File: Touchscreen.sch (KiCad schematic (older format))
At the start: 4 parts, among them P4 4pin_Cvilux_1_0mm

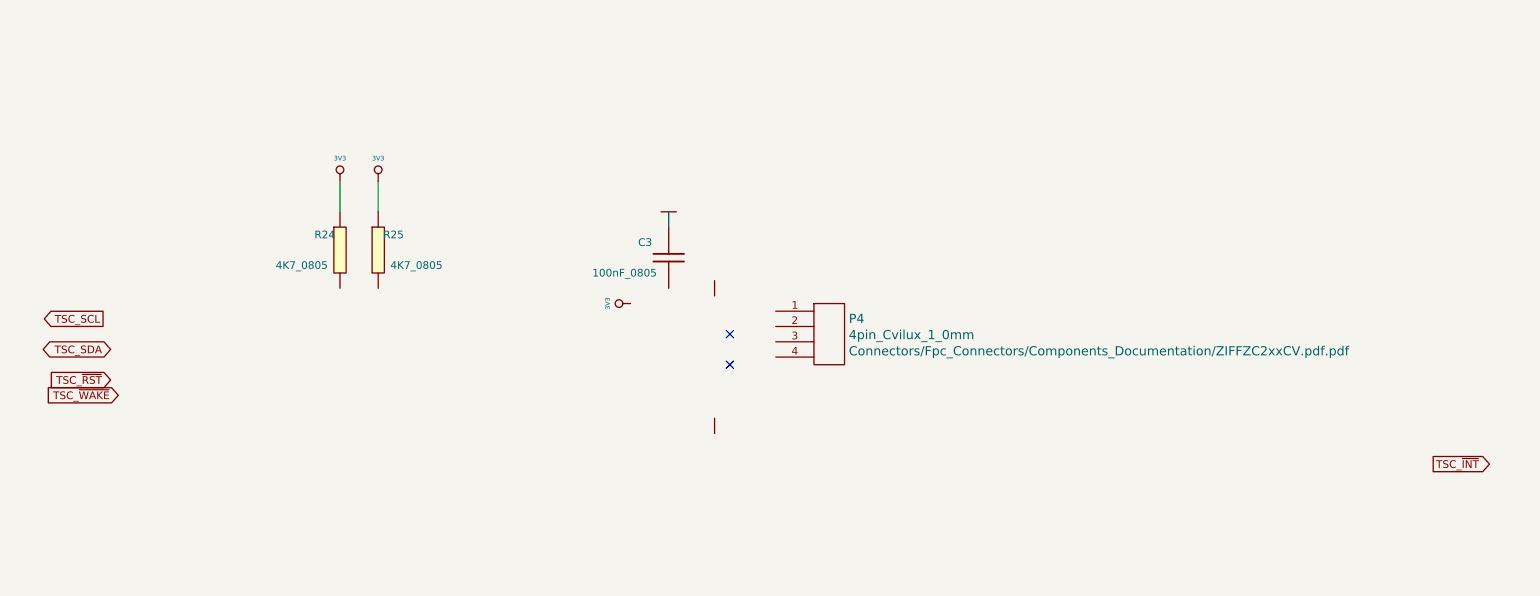
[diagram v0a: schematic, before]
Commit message: Schematic finished, needes to be rechecked, pcb finished needes to be tweeked
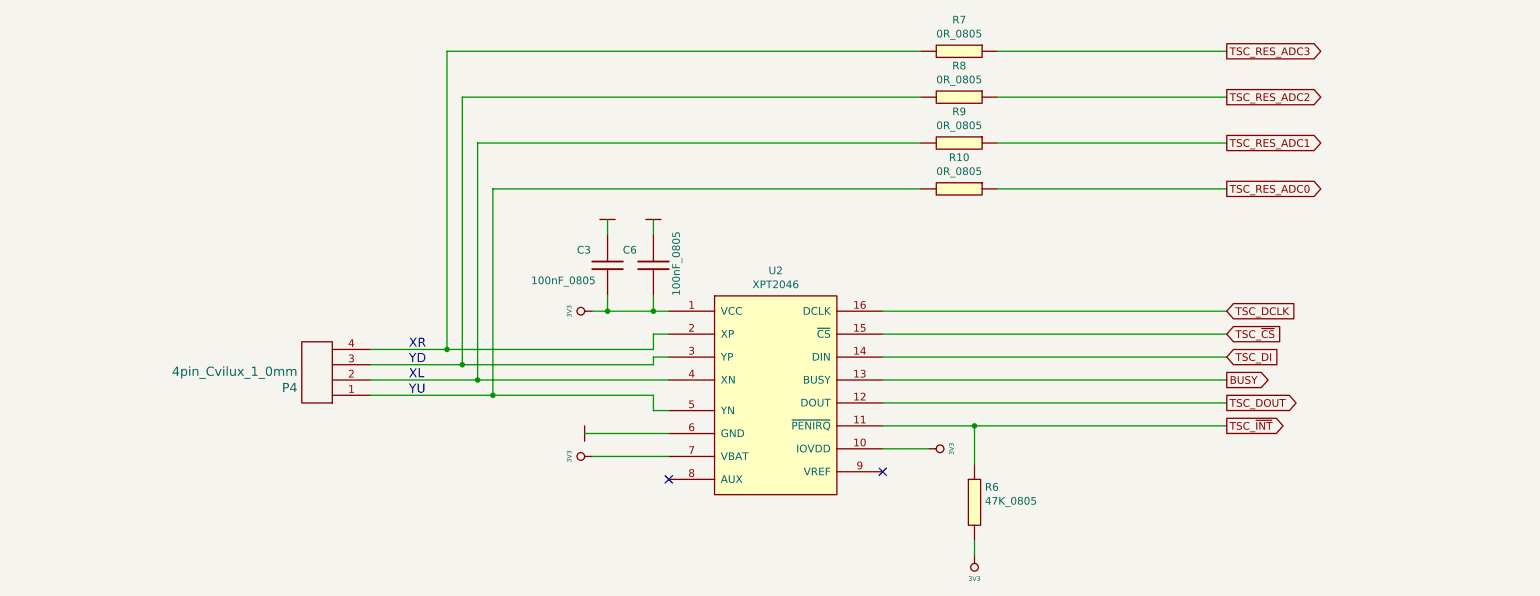
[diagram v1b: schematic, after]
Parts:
- removed R24, R25: 4K7_0805, Resistor_Smd_0805:4k7_0805, symbol 4K7_0805
- added C6: 100nF_0805, Capacitors_Smd_0805:100nF_0805, symbol 100nF_0805
- added R10, R7, R8, R9: 0R_0805, Resistor_Smd_0805:0R_0805, symbol 0R_0805
- added R6: 47K_0805, Resistor_Smd_0805:47k_0805, symbol 47K_0805
- added U2: XPT2046, Touch_Sensors:XPT2046_TSSOP16, symbol XPT2046
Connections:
- net 3V3: now also C3.2, C6.2, R6.2, U2.1 (VCC), U2.10 (IOVDD), U2.7 (VBAT)
- net GND: now also C6.1, U2.6 (GND)
- net TSC_~INT: now also R6.1, U2.11 (~PENIRQ)
- net at P4.1 (P1): now also R10.2, U2.5 (YN)
- net at P4.2 (P2): now also R9.2, U2.4 (XN)
- net at P4.3 (P3): now also R8.2, U2.3 (YP)
- net at P4.4 (P4): now also R7.2, U2.2 (XP)
- new net BUSY: U2.13 (BUSY)
- new net TSC_DCLK: U2.16 (DCLK)
- new net TSC_DI: U2.14 (DIN)
- new net TSC_DOUT: U2.12 (DOUT)
- new net TSC_RES_ADC0: R10.1
- new net TSC_RES_ADC1: R9.1
- new net TSC_RES_ADC2: R8.1
- new net TSC_RES_ADC3: R7.1
- new net TSC_~CS: U2.15 (~CS)
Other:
- note added: "XL"
- note added: "XR"
- note added: "YD"
- note added: "YU"
- moved on the sheet: C3, P4

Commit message: Corrected FPC 40pin top 0.5mm connector, generated again gerber and ps files
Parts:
- C3, C6: symbol 100nF_0805 -> Capacitors_Smd0805:100nF_0805
- P4: symbol 4pin_Cvilux_1_0mm -> Fpc_Connectors:4pin_Cvilux_1_0mm
- R10, R7, R8, R9: symbol 0R_0805 -> Resistors_Smd0805:0R_0805
- R6: symbol 47K_0805 -> Resistors_Smd0805:47K_0805
- U2: symbol XPT2046 -> Touch_Sensors:XPT2046
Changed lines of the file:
@@
-EESchema Schematic File Version 3
-LIBS:Capacitors_Smd0805
-LIBS:Capacitors_Smd_Tantal
-LIBS:Fpc_Connectors
-LIBS:Switching_Regulators
-LIBS:Diodes
-LIBS:Inductors
-LIBS:power
-LIBS:Resistors_Smd0603
-LIBS:Resistors_Smd0805
-LIBS:Symbols
-LIBS:Touch_Sensors
+EESchema Schematic File Version 4
 LIBS:TFT_LCD_4_3_AM480272H2T_V1_0-cache
 EELAYER 26 0
@@
 NoConn ~ 5200 4500
 $Comp
-L GND #PWR017
+L power1:GND #PWR017
 U 1 1 57E98920
 P 4650 4200
@@
 $EndComp
 $Comp
-L 3V3 #PWR018
+L power1:3V3 #PWR018
 U 1 1 57E99C42
 P 4700 4350
@@
 $EndComp
 $Comp
-L 100nF_0805 C3
+L Capacitors_Smd0805:100nF_0805 C3
 U 1 1 57FFFAA4
 P 4800 3100
@@
 $EndComp
 $Comp
-L GND #PWR021
+L power1:GND #PWR021
 U 1 1 57FFFB78
 P 4800 2800
@@
 $EndComp
 $Comp
-L 4pin_Cvilux_1_0mm P4
+L Fpc_Connectors:4pin_Cvilux_1_0mm P4
 U 1 1 59F3C4FD
 P 3000 3800
@@
 $EndComp
 $Comp
-L XPT2046 U2
+L Touch_Sensors:XPT2046 U2
 U 1 1 59F479B2
 P 5900 3950
@@
 $EndComp
 $Comp
-L 100nF_0805 C6
+L Capacitors_Smd0805:100nF_0805 C6
 U 1 1 59F4F1D1
 P 5100 3100
@@
 $EndComp
 $Comp
-L GND #PWR016
+L power1:GND #PWR016
 U 1 1 59F4F1D7
 P 5100 2800
@@
 Connection ~ 4800 3400
 $Comp
-L 3V3 #PWR019
+L power1:3V3 #PWR019
 U 1 1 59F4F3C1
 P 4700 3400
@@
 $EndComp
 $Comp
-L 3V3 #PWR020
+L power1:3V3 #PWR020
 U 1 1 59F4F403
 P 6900 4300
@@
 	5200 4200 4650 4200
 $Comp
-L 47K_0805 R6
+L Resistors_Smd0805:47K_0805 R6
 U 1 1 59F4F4AF
 P 7200 4650
@@
 	6600 4150 8850 4150
 $Comp
-L 3V3 #PWR022
+L power1:3V3 #PWR022
 U 1 1 59F4F59E
 P 7200 5000
@@
 XR
 $Comp
-L 0R_0805 R8
+L Resistors_Smd0805:0R_0805 R8
 U 1 1 59F50AB8
 P 7100 2000
@@
 $EndComp
 $Comp
-L 0R_0805 R7
+L Resistors_Smd0805:0R_0805 R7
 U 1 1 59F50B9D
 P 7100 1700
@@
 $EndComp
 $Comp
-L 0R_0805 R10
+L Resistors_Smd0805:0R_0805 R10
 U 1 1 59F50C3C
 P 7100 2600
@@
 $EndComp
 $Comp
-L 0R_0805 R9
+L Resistors_Smd0805:0R_0805 R9
 U 1 1 59F50C42
 P 7100 2300
